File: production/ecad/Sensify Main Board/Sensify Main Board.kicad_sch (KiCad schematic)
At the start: 9 parts

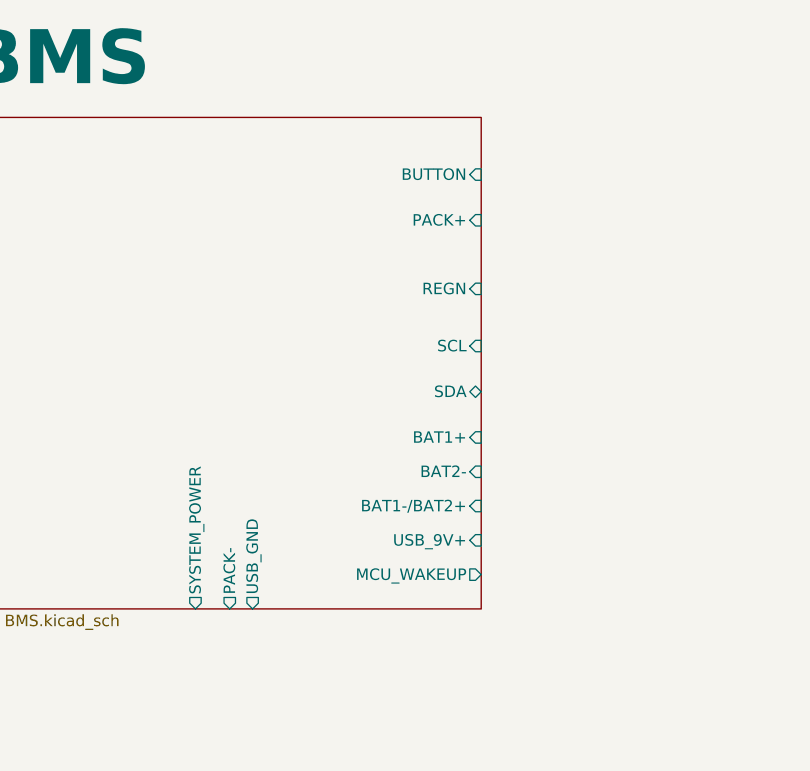
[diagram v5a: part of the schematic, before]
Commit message: v1 bms ic without charging while using functionality + changed bms hierarchical net labels
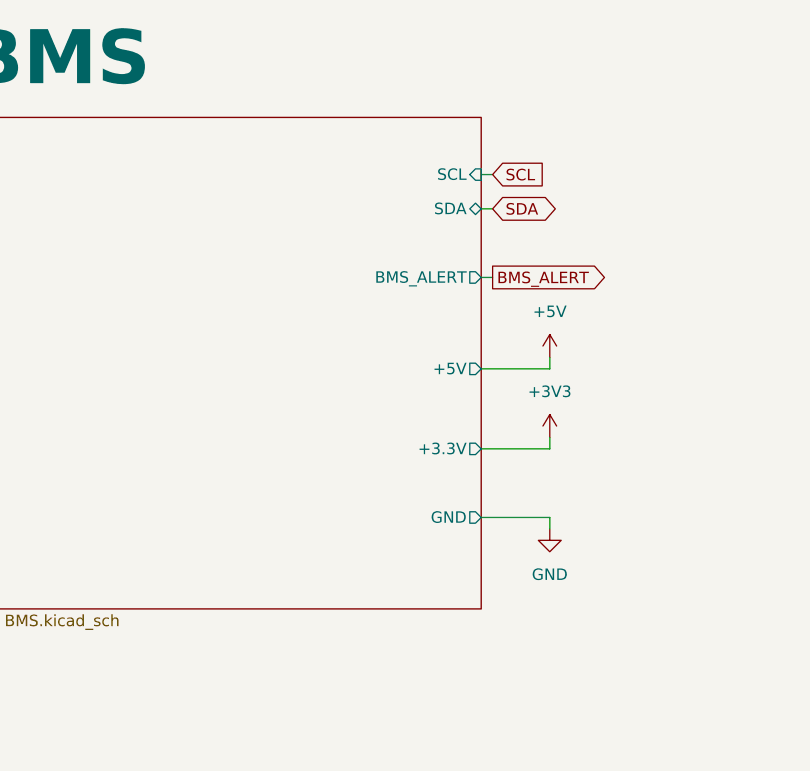
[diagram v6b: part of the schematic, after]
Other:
- sheet BMS ports: added +3.3V, +5V, BMS_ALERT, GND; removed BAT1+, BAT1-/BAT2+, BAT2-, BUTTON, MCU_WAKEUP, PACK+, PACK-, REGN, SYSTEM_POWER, USB_9V+, USB_GND
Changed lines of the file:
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@@
+    (stroke (width 0) (type default))
+  )
+  (wire (pts (xy 109.22 93.98) (xy 116.84 93.98))
+    (stroke (width 0) (type default))
+  )
+  (wire (pts (xy 109.22 77.47) (xy 116.84 77.47))
+    (stroke (width 0) (type default))
+  )
+  (wire (pts (xy 116.84 93.98) (xy 116.84 95.25))
     (stroke (width 0) (type default))
   )
@@
     (stroke (width 0) (type default))
   )
+  (wire (pts (xy 109.22 86.36) (xy 116.84 86.36))
+    (stroke (width 0) (type default))
+  )
   (wire (pts (xy 111.76 190.5) (xy 113.03 190.5))
     (stroke (width 0) (type default))
@@
     (stroke (width 0) (type default))
   )
+  (wire (pts (xy 109.22 59.69) (xy 110.49 59.69))
+    (stroke (width 0) (type default))
+  )
   (wire (pts (xy 181.61 124.46) (xy 185.42 124.46))
     (stroke (width 0) (type default))
@@
     (stroke (width 0) (type default))
   )
+  (wire (pts (xy 109.22 67.31) (xy 110.49 67.31))
+    (stroke (width 0) (type default))
+  )
   (wire (pts (xy 309.88 55.88) (xy 313.69 55.88))
     (stroke (width 0) (type default))
@@
     (stroke (width 0) (type default))
   )
+  (wire (pts (xy 109.22 55.88) (xy 110.49 55.88))
+    (stroke (width 0) (type default))
+  )
   (wire (pts (xy 265.43 238.76) (xy 274.32 238.76))
     (stroke (width 0) (type default))
@@
     (stroke (width 0) (type default))
   )
+  (wire (pts (xy 116.84 76.2) (xy 116.84 77.47))
+    (stroke (width 0) (type default))
+  )
   (wire (pts (xy 173.99 130.81) (xy 185.42 130.81))
     (stroke (width 0) (type default))
@@
   )
   (wire (pts (xy 312.42 86.36) (xy 313.69 86.36))
+    (stroke (width 0) (type default))
+  )
+  (wire (pts (xy 116.84 85.09) (xy 116.84 86.36))
     (stroke (width 0) (type default))
   )
@@
     )
   )
+  (global_label "BMS_ALERT" (shape output) (at 110.49 67.31 0) (fields_autoplaced)
+    (effects (font (size 1.27 1.27)) (justify left))
+    (property "Intersheetrefs" "${INTERSHEET_REFS}" (at 123.877 67.31 0)
+      (effects (font (size 1.27 1.27)) (justify left) hide)
+    )
+  )
+  (global_label "SDA" (shape bidirectional) (at 110.49 59.69 0) (fields_autoplaced)
+    (effects (font (size 1.27 1.27)) (justify left))
+    (property "Intersheetrefs" "${INTERSHEET_REFS}" (at 118.1546 59.69 0)
+      (effects (font (size 1.27 1.27)) (justify left) hide)
+    )
+  )
   (global_label "SDA" (shape bidirectional) (at 184.15 156.21 180) (fields_autoplaced)
     (effects (font (size 1.27 1.27)) (justify right))
@@
     )
   )
+  (global_label "SCL" (shape input) (at 110.49 55.88 0) (fields_autoplaced)
+    (effects (font (size 1.27 1.27)) (justify left))
+    (property "Intersheetrefs" "${INTERSHEET_REFS}" (at 116.9828 55.88 0)
+      (effects (font (size 1.27 1.27)) (justify left) hide)
+    )
+  )
   (global_label "SDA" (shape bidirectional) (at 312.42 77.47 180) (fields_autoplaced)
     (effects (font (size 1.27 1.27)) (justify right))
@@
     )
   )
+  (symbol (lib_id "power:+5V") (at 116.84 76.2 0) (unit 1)
+    (in_bom yes) (on_board yes) (dnp no) (fields_autoplaced)
+    (property "Reference" "#PWR077" (at 116.84 80.01 0)
+      (effects (font (size 1.27 1.27)) hide)
+    )
+    (property "Value" "+5V" (at 116.84 71.12 0)
+      (effects (font (size 1.27 1.27)))
+    )
+    (property "Footprint" "" (at 116.84 76.2 0)
+      (effects (font (size 1.27 1.27)) hide)
+    )
+    (property "Datasheet" "" (at 116.84 76.2 0)
+      (effects (font (size 1.27 1.27)) hide)
+    )
+    (pin "1")
+    (instances
+      (project "Sensify Main Board"
+        (path "/9a7ba7c3-7d28-4a83-bdbc-38fbff59fcbe"
+          (reference "#PWR077") (unit 1)
+        )
+      )
+    )
+  )
   (symbol (lib_id "power:GND") (at 116.84 205.74 0) (unit 1)
     (in_bom yes) (on_board yes) (dnp no) (fields_autoplaced)
@@
     )
   )
+  (symbol (lib_id "power:GND") (at 116.84 95.25 0) (unit 1)
+    (in_bom yes) (on_board yes) (dnp no) (fields_autoplaced)
+    (property "Reference" "#PWR080" (at 116.84 101.6 0)
+      (effects (font (size 1.27 1.27)) hide)
+    )
+    (property "Value" "GND" (at 116.84 100.33 0)
+      (effects (font (size 1.27 1.27)))
+    )
+    (property "Footprint" "" (at 116.84 95.25 0)
+      (effects (font (size 1.27 1.27)) hide)
+    )
+    (property "Datasheet" "" (at 116.84 95.25 0)
+      (effects (font (size 1.27 1.27)) hide)
+    )
+    (pin "1")
+    (instances
+      (project "Sensify Main Board"
+        (path "/9a7ba7c3-7d28-4a83-bdbc-38fbff59fcbe"
+          (reference "#PWR080") (unit 1)
+        )
+      )
+    )
+  )
   (symbol (lib_id "power:+5V") (at 309.88 55.88 0) (unit 1)
     (in_bom yes) (on_board yes) (dnp no) (fields_autoplaced)
@@
         (path "/9a7ba7c3-7d28-4a83-bdbc-38fbff59fcbe"
           (reference "#PWR02") (unit 1)
+        )
+      )
+    )
+  )
+  (symbol (lib_id "power:+3V3") (at 116.84 85.09 0) (unit 1)
+    (in_bom yes) (on_board yes) (dnp no) (fields_autoplaced)
+    (property "Reference" "#PWR079" (at 116.84 88.9 0)
+      (effects (font (size 1.27 1.27)) hide)
+    )
+    (property "Value" "+3V3" (at 116.84 80.01 0)
+      (effects (font (size 1.27 1.27)))
+    )
+    (property "Footprint" "" (at 116.84 85.09 0)
+      (effects (font (size 1.27 1.27)) hide)
+    )
+    (property "Datasheet" "" (at 116.84 85.09 0)
+      (effects (font (size 1.27 1.27)) hide)
+    )
+    (pin "1")
+    (instances
+      (project "Sensify Main Board"
+        (path "/9a7ba7c3-7d28-4a83-bdbc-38fbff59fcbe"
+          (reference "#PWR079") (unit 1)
         )
       )
@@
       (effects (font (size 1.27 1.27)) (justify left top))
     )
-    (pin "SCL" input (at 109.22 74.93 0)
+    (pin "SCL" input (at 109.22 55.88 0)
       (effects (font (size 1.27 1.27)) (justify right))
     )
-    (pin "SDA" bidirectional (at 109.22 80.01 0)
+    (pin "SDA" bidirectional (at 109.22 59.69 0)
       (effects (font (size 1.27 1.27)) (justify right))
     )
-    (pin "REGN" input (at 109.22 68.58 0)
+    (pin "GND" output (at 109.22 93.98 0)
       (effects (font (size 1.27 1.27)) (justify right))
     )
-    (pin "BAT1+" input (at 109.22 85.09 0)
+    (pin "BMS_ALERT" output (at 109.22 67.31 0)
       (effects (font (size 1.27 1.27)) (justify right))
     )
-    (pin "BAT2-" input (at 109.22 88.9 0)
+    (pin "+5V" output (at 109.22 77.47 0)
       (effects (font (size 1.27 1.27)) (justify right))
     )
-    (pin "BAT1-{slash}BAT2+" input (at 109.22 92.71 0)
+    (pin "+3.3V" output (at 109.22 86.36 0)
       (effects (font (size 1.27 1.27)) (justify right))
     )
-    (pin "USB_9V+" input (at 109.22 96.52 0)
-      (effects (font (size 1.27 1.27)) (justify right))
-    )
-    (pin "PACK+" input (at 109.22 60.96 0)
-      (effects (font (size 1.27 1.27)) (justify right))
-    )
-    (pin "BUTTON" input (at 109.22 55.88 0)
-      (effects (font (size 1.27 1.27)) (justify right))
-    )
-    (pin "MCU_WAKEUP" output (at 109.22 100.33 0)
-      (effects (font (size 1.27 1.27)) (justify right))
-    )
-    (pin "SYSTEM_POWER" output (at 77.47 104.14 270)
-      (effects (font (size 1.27 1.27)) (justify left))
-    )
-    (pin "PACK-" output (at 81.28 104.14 270)
-      (effects (font (size 1.27 1.27)) (justify left))
-    )
-    (pin "USB_GND" output (at 83.82 104.14 270)
-      (effects (font (size 1.27 1.27)) (justify left))
-    )
-    (instances
+    (instances

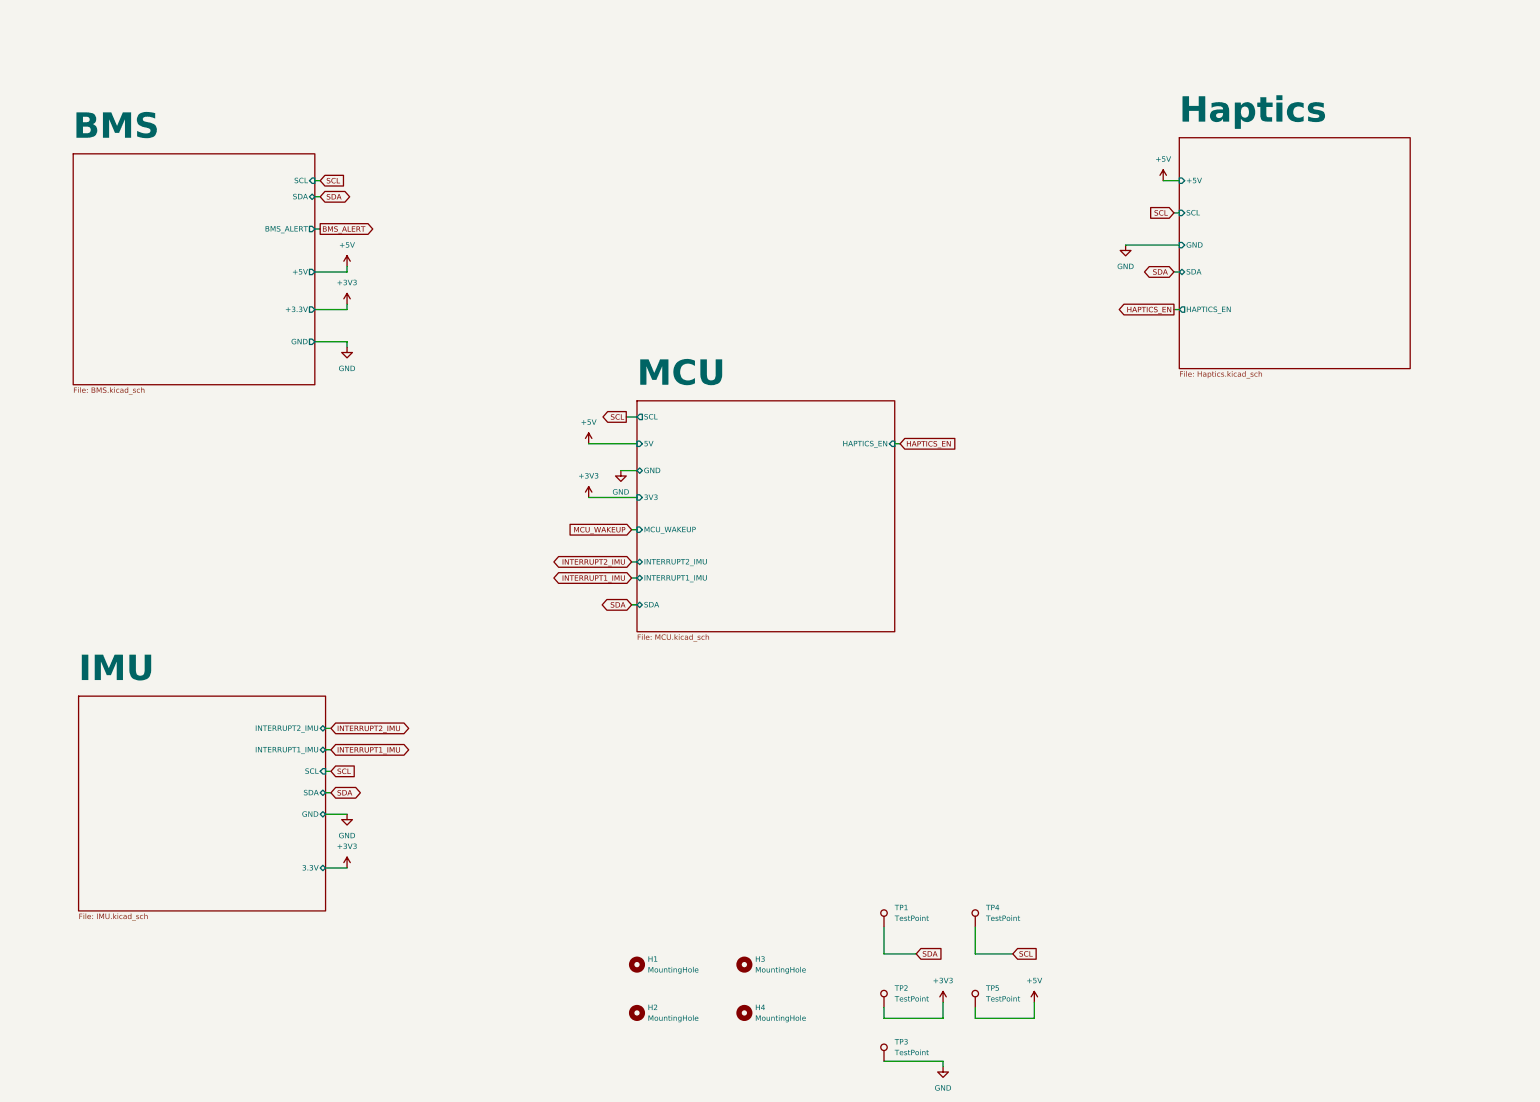
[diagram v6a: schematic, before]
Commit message: Updated MCU Schematic
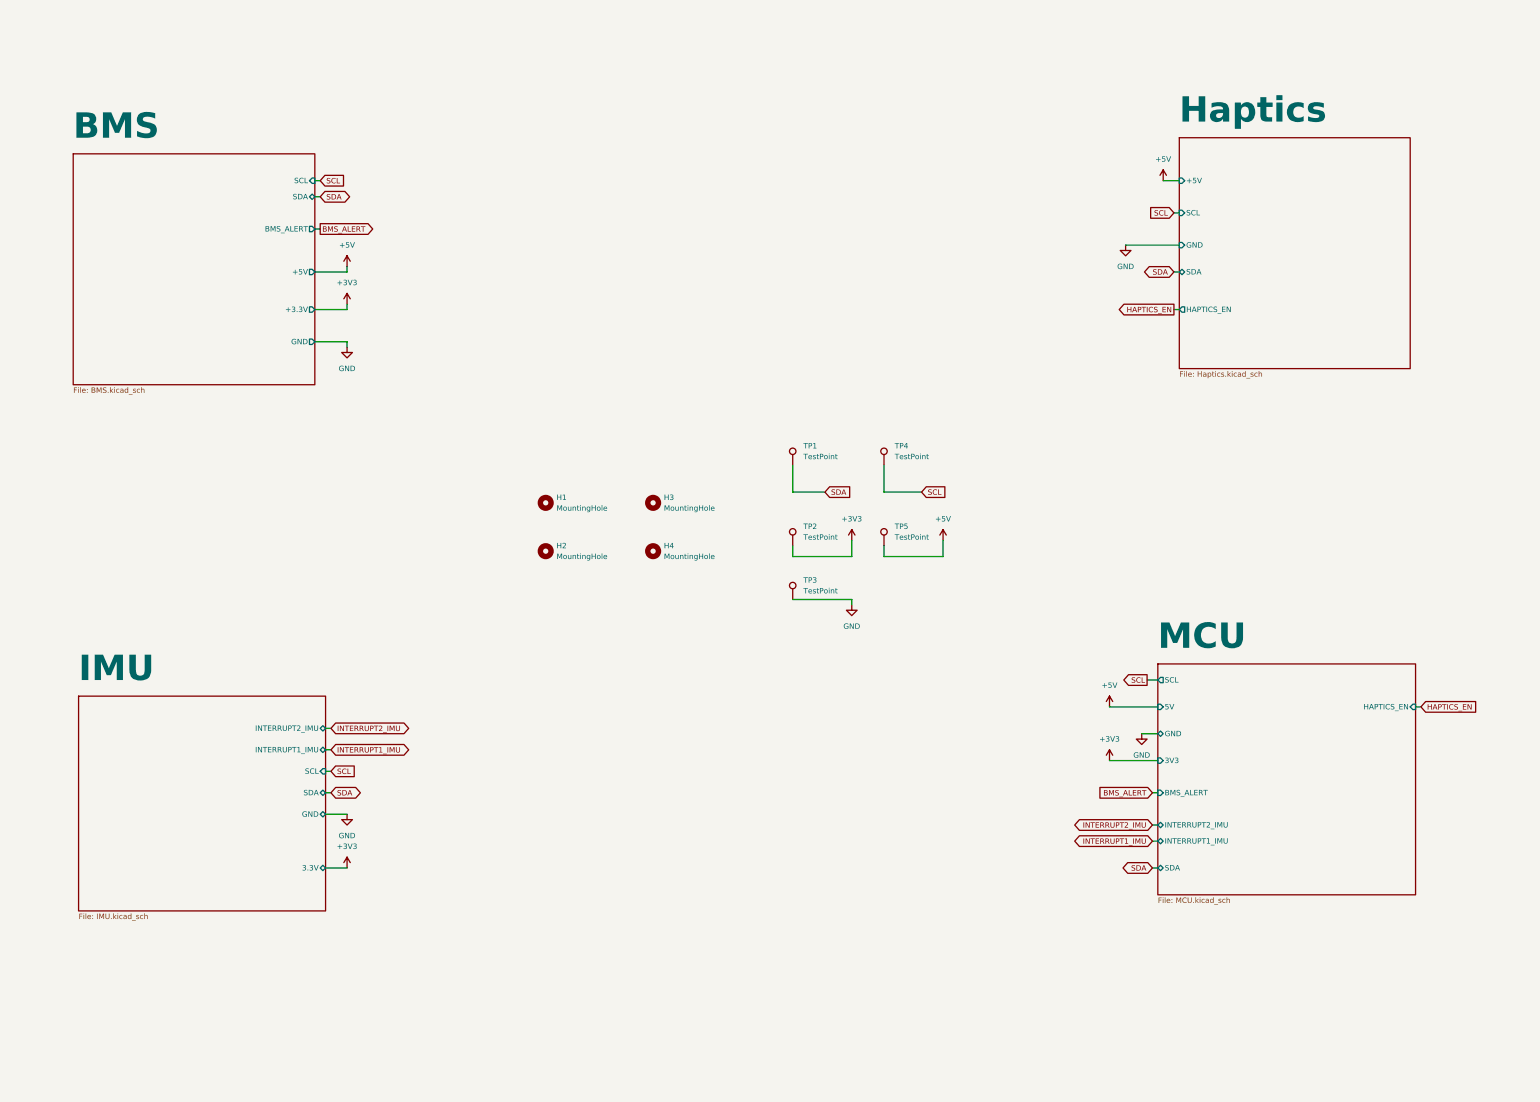
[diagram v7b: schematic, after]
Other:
- sheet MCU ports: added BMS_ALERT; removed MCU_WAKEUP
- moved on the sheet: H1, H2, H3, H4, TP1, TP2, TP3, TP4, TP5

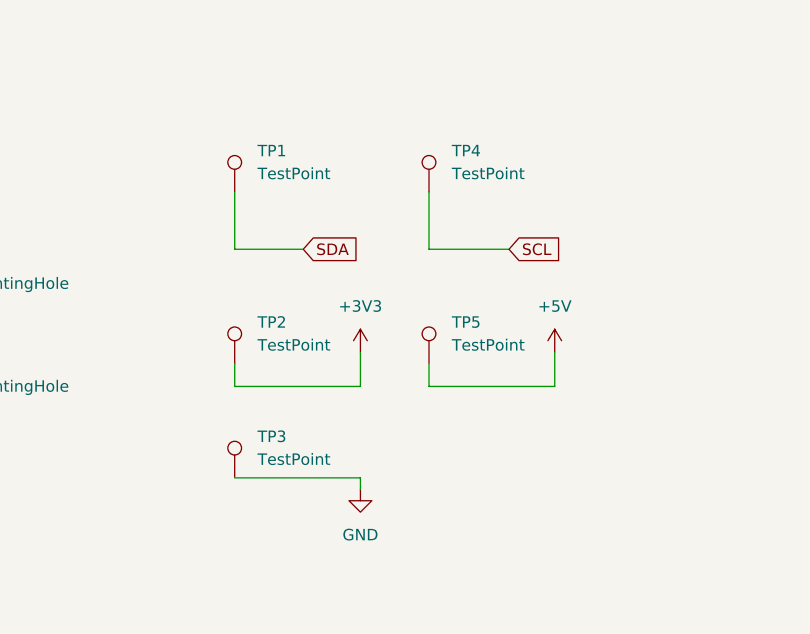
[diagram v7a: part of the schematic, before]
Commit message: Added Labels to Test Points
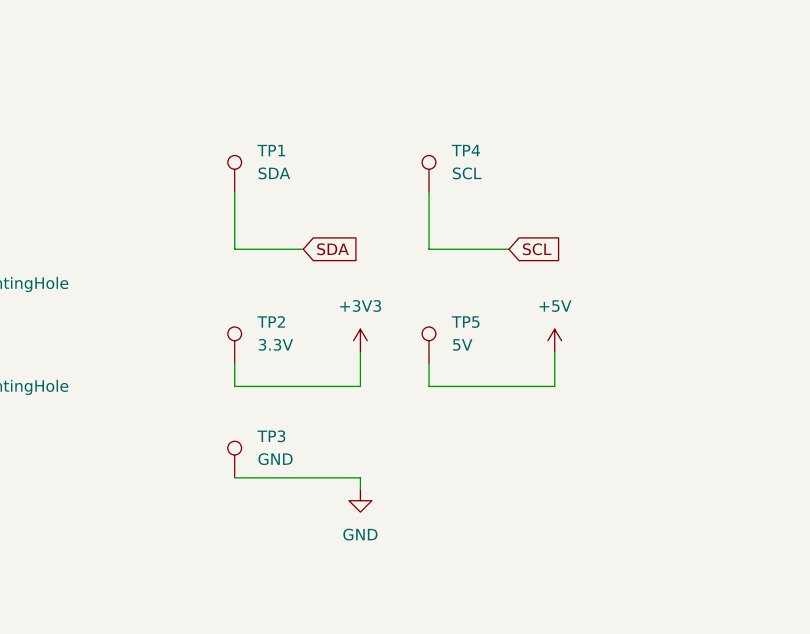
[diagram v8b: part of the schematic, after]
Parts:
- TP1: value TestPoint -> SDA
- TP2: value TestPoint -> 3.3V
- TP3: value TestPoint -> GND
- TP4: value TestPoint -> SCL
- TP5: value TestPoint -> 5V
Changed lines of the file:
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@@
       (effects (font (size 1.27 1.27)) (justify left))
     )
-    (property "Value" "TestPoint" (at 224.79 140.208 0)
+    (property "Value" "3.3V" (at 224.79 140.208 0)
       (effects (font (size 1.27 1.27)) (justify left))
     )
@@
       (effects (font (size 1.27 1.27)) (justify left))
     )
-    (property "Value" "TestPoint" (at 224.79 121.158 0)
+    (property "Value" "SDA" (at 224.79 121.158 0)
       (effects (font (size 1.27 1.27)) (justify left))
     )
@@
       (effects (font (size 1.27 1.27)) (justify left))
     )
-    (property "Value" "TestPoint" (at 224.79 152.908 0)
+    (property "Value" "GND" (at 224.79 152.908 0)
       (effects (font (size 1.27 1.27)) (justify left))
     )
@@
       (effects (font (size 1.27 1.27)) (justify left))
     )
-    (property "Value" "TestPoint" (at 246.38 140.208 0)
+    (property "Value" "5V" (at 246.38 140.208 0)
       (effects (font (size 1.27 1.27)) (justify left))
     )
@@
       (effects (font (size 1.27 1.27)) (justify left))
     )
-    (property "Value" "TestPoint" (at 246.38 121.158 0)
-      (effects (font (size 1.27 1.27)) (justify left))
-    )
+    (property "Value" "SCL" (at 246.38 121.158 0)
+      (effects (font (size 1.27 1.27)) (justify left))
+    )
